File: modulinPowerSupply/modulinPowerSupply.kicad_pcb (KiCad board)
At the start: 2 copper layers, 57.1 x 111.8 mm, 33 parts, among them J1 Barrel_Jack_Switch, J2 Screw_Terminal_01x04, U1 LM7812_TO220, U2 LM7912_TO220, U5 LM7805_TO220

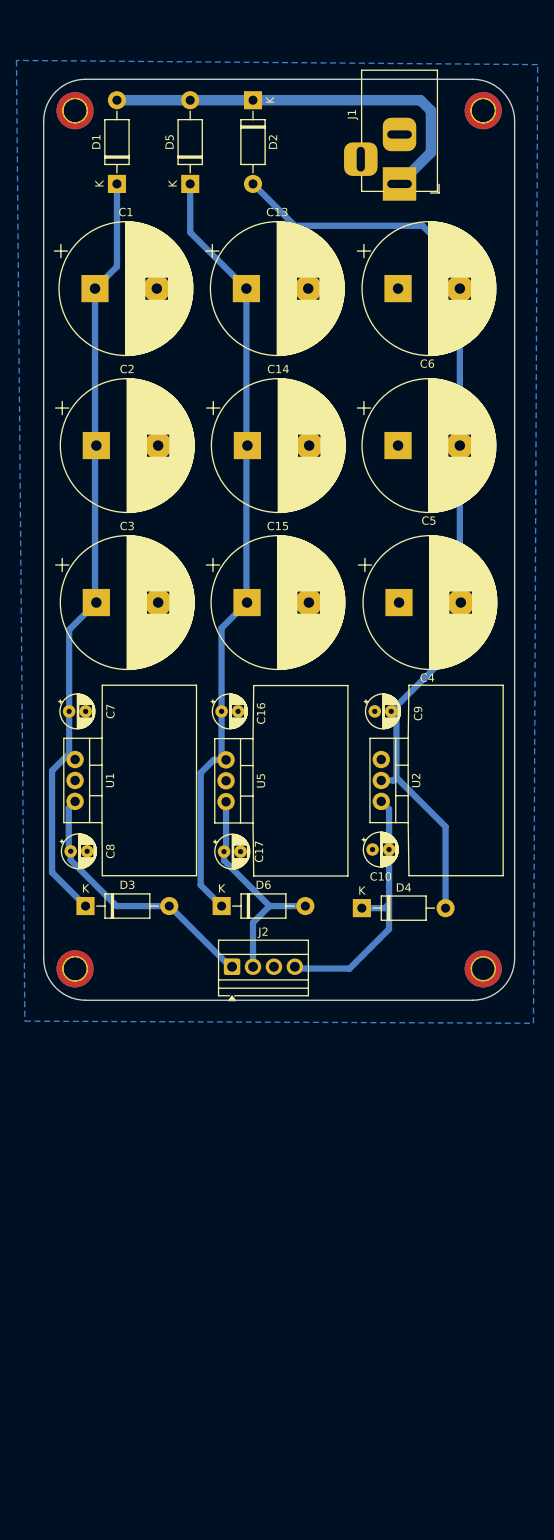
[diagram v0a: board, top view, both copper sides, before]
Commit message: Write out envelope circuit and make PCB, edit PSU
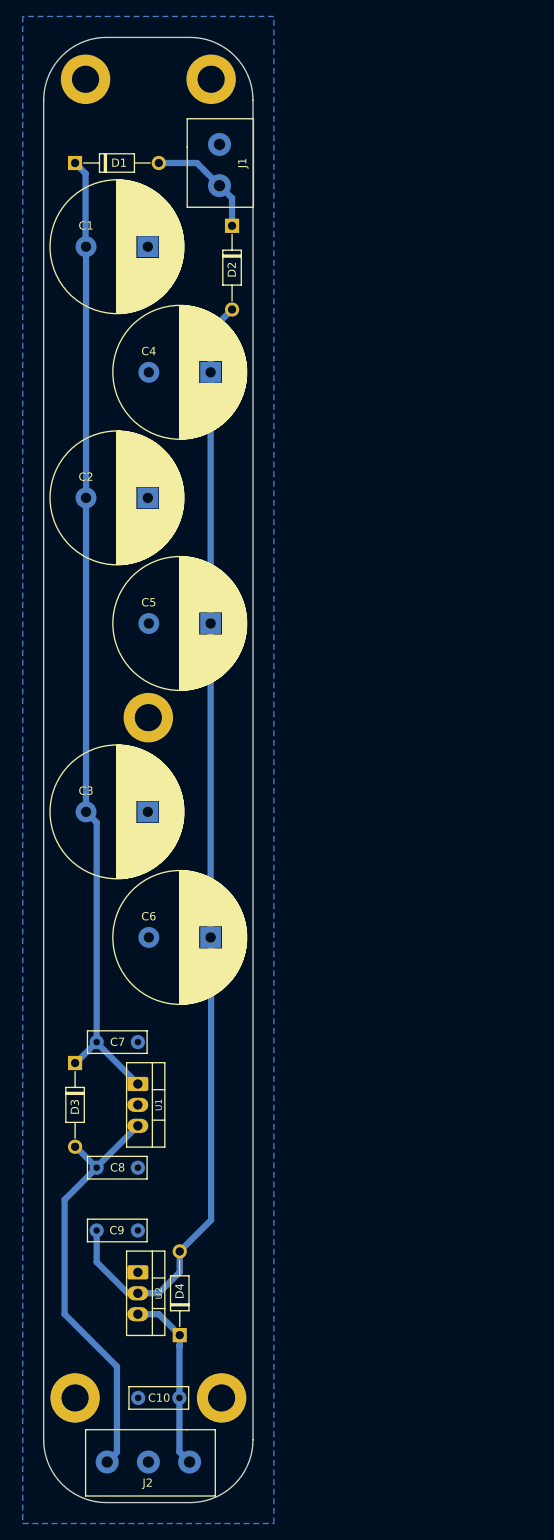
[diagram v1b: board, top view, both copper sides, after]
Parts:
- removed ? (x3): , 
- removed C13, C14, C15: 4700uF, Capacitor_THT:CP_Radial_D16.0mm_P7.50mm
- removed C16, C17: 1uF, Capacitor_THT:CP_Radial_D4.0mm_P2.00mm
- removed D5, D6: 1N4001, Diode_THT:D_DO-41_SOD81_P10.16mm_Horizontal
- removed the REF** at (29.2, 24.1)
- removed the REF** at (78.7, 24.1)
- removed the REF** at (78.7, 128.3)
- removed the REF** at (29.2, 128.3)
- removed U5: LM7805_TO220, Package_TO_SOT_THT:TO-220-3_Vertical
- added REF**: MountingHole_M3_CNC, User:MountingHole_M3_CNC, F.Cu at (38.1, 97.8)
- added REF**: MountingHole_M3_CNC, User:MountingHole_M3_CNC, F.Cu at (45.7, 20.3)
- added REF**: MountingHole_M3_CNC, User:MountingHole_M3_CNC, F.Cu at (30.5, 20.3)
- added REF**: MountingHole_M3_CNC, User:MountingHole_M3_CNC, F.Cu at (29.2, 180.3)
- added REF**: MountingHole_M3_CNC, User:MountingHole_M3_CNC, F.Cu at (47.0, 180.3)
- C1, C2, C3, C4, C5, C6: footprint Capacitor_THT:CP_Radial_D16.0mm_P7.50mm -> User:C_Radial_Polarized_P7.50mm_CNC
- C10, C7, C8, C9: footprint Capacitor_THT:CP_Radial_D4.0mm_P2.00mm -> User:C_Rect_P5.00mm_CNC
- D1, D2, D3, D4: footprint Diode_THT:D_DO-41_SOD81_P10.16mm_Horizontal -> User:D_P10.16mm_CNC
- J1: value Barrel_Jack_Switch -> Screw_Terminal_01x02; footprint Connector_BarrelJack:BarrelJack_Horizontal -> User:TerminalBlock_1x2_CNC
- J2: value Screw_Terminal_01x04 -> Screw_Terminal_01x03; footprint TerminalBlock:TerminalBlock_Xinya_XY308-2.54-4P_1x04_P2.54mm_Horizontal -> User:TerminalBlock_1x3_CNC
- U1, U2: footprint Package_TO_SOT_THT:TO-220-3_Vertical -> User:TO-220_CNC
- moved C6 84.3 mm to (38.2, 124.5)
- moved C10 72.4 mm to (36.9, 180.3)
- moved U2 71.2 mm to (36.8, 167.6)
- moved C9 69.2 mm to (36.8, 160.0), turned to 180 degrees
- moved J2 60.3 mm to (43.1, 188.1), turned to 180 degrees
- moved D4 56.3 mm to (41.9, 172.7), turned to 90 degrees
- moved U1 42.6 mm to (36.8, 144.8)
- moved C4 41.3 mm to (38.2, 55.9)
- moved C7 40.3 mm to (31.8, 137.2)
- moved C8 38.5 mm to (31.8, 152.4)
- moved C5 37.2 mm to (38.2, 86.4)
- moved C3 25.4 mm to (30.5, 109.2)
- moved J1 22.4 mm to (46.7, 28.2)
- moved D3 19.1 mm to (29.2, 139.7), turned to -90 degrees
- moved D2 15.5 mm to (48.3, 38.1)
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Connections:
- J1 pad 1: Net-(D1-A) -> GND
- J1 pad 2: GND -> Net-(D1-A)
- J2 pad 1: +12V -> -12V
- J2 pad 2: +5V -> GND
- J2 pad 3: GND -> +12V
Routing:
- net Net-(D5-K): track 95.2 -> 0.00 mm
- net Net-(D1-A): track 49.1 -> 14.0 mm
- net +5V: track 27.8 -> 0.00 mm
- net Net-(D1-K): track 93.7 -> 119.0 mm
- net Net-(D2-A): track 115.6 -> 137.0 mm
- net +12V: track 32.6 -> 51.3 mm
- net -12V: track 32.8 -> 22.1 mm
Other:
- board size 57.1 x 111.8 mm -> 25.4 x 177.8 mm
